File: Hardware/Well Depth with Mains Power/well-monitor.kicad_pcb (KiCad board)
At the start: 2 copper layers, 1 part, among them U1 ATmega328P-PU

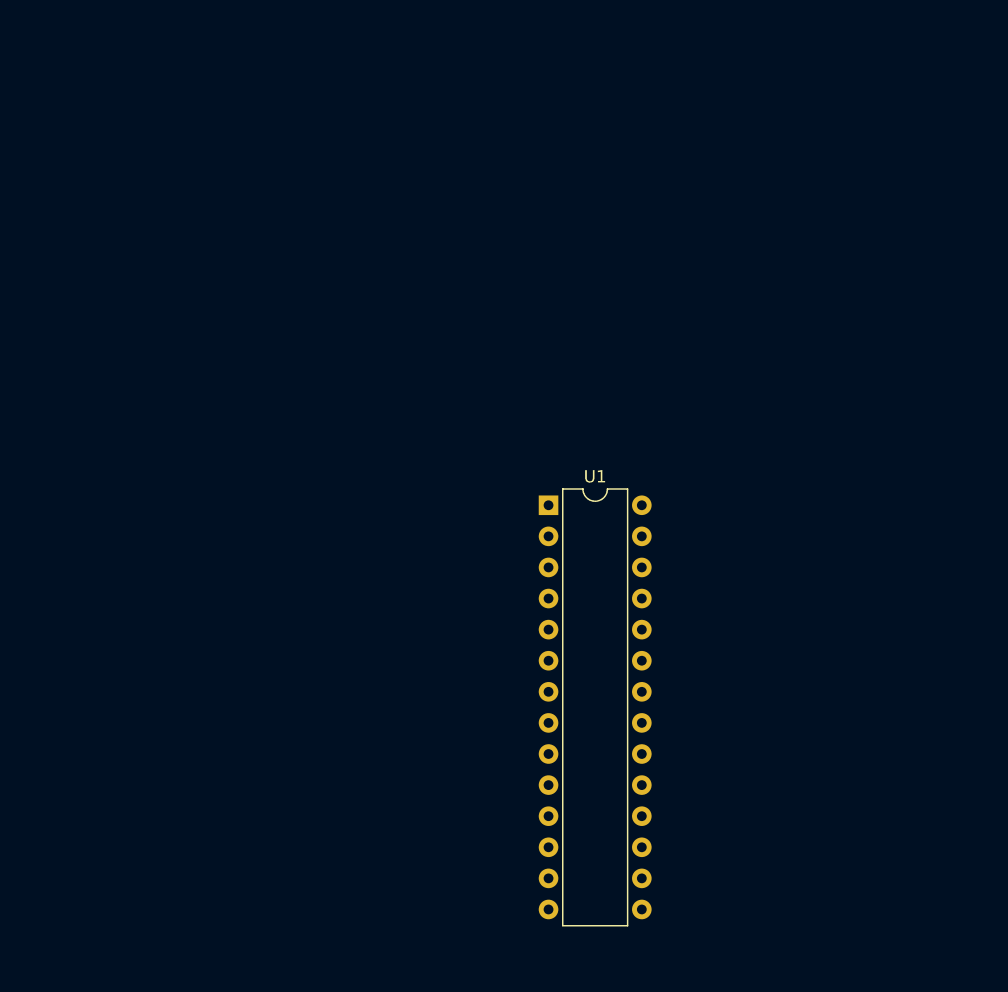
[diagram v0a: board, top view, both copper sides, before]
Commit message: First pass routing and DRC/ERC pass
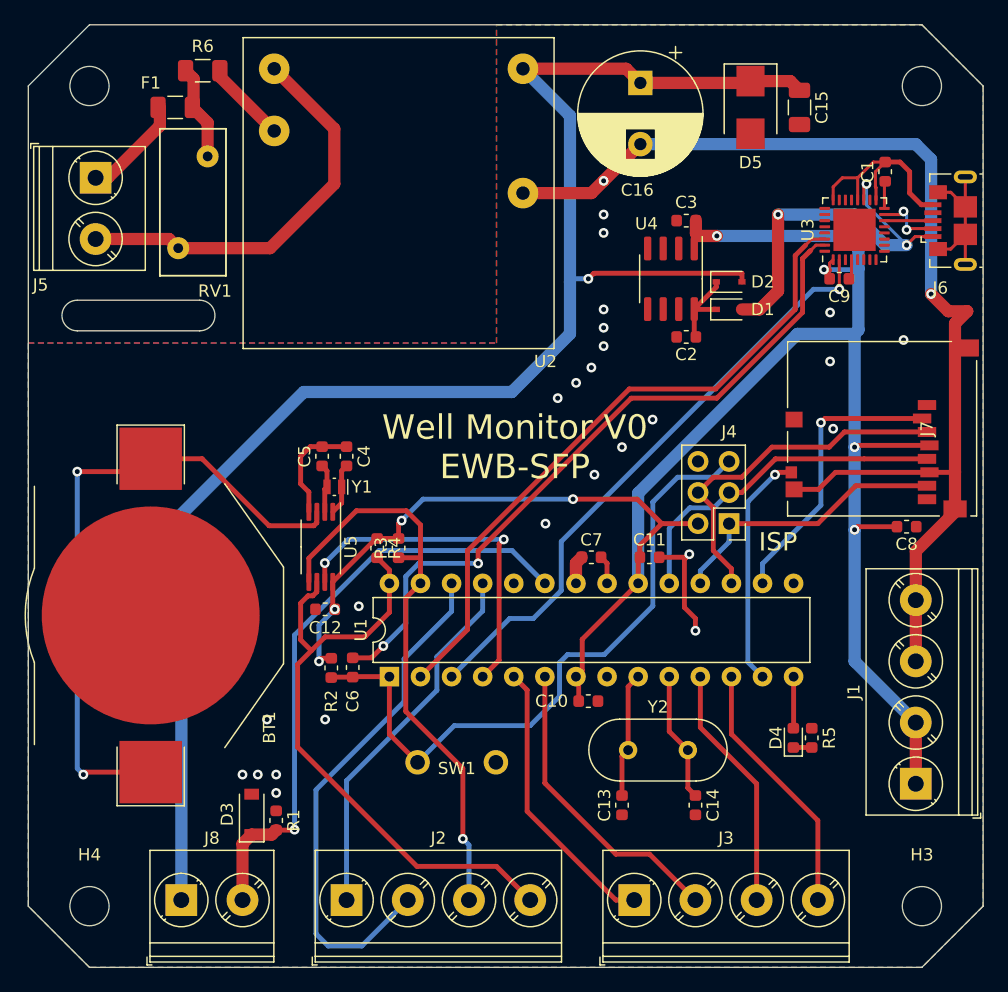
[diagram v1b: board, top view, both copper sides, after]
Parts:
- added BT1: Battery_Cell, well-monitor:BatteryHolder_Keystone_3002_1x2032, F.Cu at (105.0, 92.2)
- added C1: 1u, Capacitor_SMD:C_0603_1608Metric, F.Cu at (165.0, 56.0)
- added C10: 100n, Capacitor_SMD:C_0603_1608Metric, F.Cu at (140.8, 99.2)
- added C11: 100n, Capacitor_SMD:C_0603_1608Metric, F.Cu at (145.8, 87.5)
- added C12: 100n, Capacitor_SMD:C_0603_1608Metric, F.Cu at (119.2, 91.8)
- added C13: 10p, Capacitor_SMD:C_0603_1608Metric, F.Cu at (143.5, 107.8)
- added C14: 10p, Capacitor_SMD:C_0603_1608Metric, F.Cu at (149.5, 107.8)
- added C15: 1u, Capacitor_SMD:C_1206_3216Metric, F.Cu at (158.0, 50.8)
- added C16: 68u, Capacitor_THT:CP_Radial_D10.0mm_P5.00mm, F.Cu at (145.0, 48.8)
- added C2: 1u, Capacitor_SMD:C_0603_1608Metric, F.Cu at (148.8, 69.5)
- added C3: 1u, Capacitor_SMD:C_0603_1608Metric, F.Cu at (148.8, 60.0)
- added C4: 10p, Capacitor_SMD:C_0603_1608Metric, F.Cu at (121.0, 79.2)
- added C5: 10p, Capacitor_SMD:C_0603_1608Metric, F.Cu at (119.0, 79.2)
- added C6: 100n, Capacitor_SMD:C_0603_1608Metric, F.Cu at (121.5, 96.5)
- added C7: 100n, Capacitor_SMD:C_0603_1608Metric, F.Cu at (141.0, 87.5)
- added C8: 100n, Capacitor_SMD:C_0603_1608Metric, F.Cu at (166.8, 85.0)
- added C9: 100n, Capacitor_SMD:C_0603_1608Metric, F.Cu at (161.2, 64.8)
- added D1: CUS10S30, Diode_SMD:D_SOD-323, F.Cu at (152.2, 67.2)
- added D2: CUS10S30, Diode_SMD:D_SOD-323, F.Cu at (152.2, 65.0)
- added D3: 3.3, Diode_SMD:D_SOD-123, F.Cu at (113.2, 108.5)
- added D4: LED_Small, LED_SMD:LED_0603_1608Metric, F.Cu at (157.5, 102.2)
- added D5: SMBJ30A, Diode_SMD:D_SMB, F.Cu at (154.0, 50.8)
- added F1: 1, Fuse:Fuse_1206_3216Metric, F.Cu at (107.0, 50.8)
- added H1: MountingHole, MountingHole:MountingHole_3.2mm_M3, F.Cu at (100.0, 49.0)
- added H2: MountingHole, MountingHole:MountingHole_3.2mm_M3, F.Cu at (168.0, 49.0)
- added H3: MountingHole, MountingHole:MountingHole_3.2mm_M3, F.Cu at (168.0, 116.0)
- added H4: MountingHole, MountingHole:MountingHole_3.2mm_M3, F.Cu at (100.0, 116.0)
- added J1: Screw_Terminal_01x04, well-monitor:TerminalBlock_Phoenix_PT-1,5-4-5.0-H_1x04_P5.00mm_Horizontal, F.Cu at (167.5, 106.0)
- added J2: Screw_Terminal_01x04, well-monitor:TerminalBlock_Phoenix_PT-1,5-4-5.0-H_1x04_P5.00mm_Horizontal, F.Cu at (121.0, 115.5)
- added J3: Screw_Terminal_01x04, well-monitor:TerminalBlock_Phoenix_PT-1,5-4-5.0-H_1x04_P5.00mm_Horizontal, F.Cu at (144.5, 115.5)
- added J4: ISP Header, Connector_PinHeader_2.54mm:PinHeader_2x03_P2.54mm_Vertical, F.Cu at (152.2, 84.8)
- added J5: Screw_Terminal_01x02, well-monitor:TerminalBlock_Phoenix_PT-1,5-2-5.0-H_1x02_P5.00mm_Horizontal, F.Cu at (100.5, 56.5)
- added J6: USB_B_Micro, well-monitor:USB_Micro-B_GCT_USB3076-30-A, F.Cu at (170.3, 60.0)
- added J7: Micro_SD_Card, well-monitor:MEM2051-00-195-00-A, F.Cu at (164.8, 77.0)
- added J8: SENSOR, well-monitor:TerminalBlock_Phoenix_PT-1,5-2-5.0-H_1x02_P5.00mm_Horizontal, F.Cu at (107.5, 115.5)
- added R1: 150, Resistor_SMD:R_0603_1608Metric, F.Cu at (115.2, 109.0)
- added R2: 10k, Resistor_SMD:R_0603_1608Metric, F.Cu at (119.8, 96.5)
- added R3: 10k, Resistor_SMD:R_0603_1608Metric, F.Cu at (125.2, 86.8)
- added R4: 10k, Resistor_SMD:R_0603_1608Metric, F.Cu at (123.5, 86.8)
- added R5: 330, Resistor_SMD:R_0603_1608Metric, F.Cu at (159.0, 102.2)
- added R6: 12, Resistor_SMD:R_1206_3216Metric, F.Cu at (109.2, 47.8)
- added RV1: S10K350, Varistor:RV_Disc_D12mm_W5.4mm_P7.5mm, F.Cu at (107.2, 62.2)
- added SW1: SW_Push, well-monitor:PTS636-SP43-LFS, F.Cu at (130.0, 104.2)
- added U2: PSK-5D-24, well-monitor:PSK-5D-24, F.Cu at (125.2, 57.8)
- added U3: CY7C65213A-32LTXI, Package_DFN_QFN:QFN-32-1EP_5x5mm_P0.5mm_EP3.45x3.45mm, F.Cu at (162.5, 60.8)
- added U4: L78L33_SO8, Package_SO:SOIC-8_3.9x4.9mm_P1.27mm, F.Cu at (147.5, 64.8)
- added U5: MCP7940N-xMS, Package_SO:TSSOP-8_4.4x3mm_P0.65mm, F.Cu at (118.9, 86.7)
- added Y1: 32.768, Crystal:Crystal_SMD_MicroCrystal_CM9V-T1A-2Pin_1.6x1.0mm, F.Cu at (120.0, 81.8)
- added Y2: 16Meg, Crystal:Crystal_HC49-U_Vertical, F.Cu at (144.0, 103.2)
- moved U1 19.1 mm to (124.5, 97.2), turned to 90 degrees
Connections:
- U1 pad 1: (no net) -> /~RESET
- U1 pad 10: (no net) -> Net-(C14-Pad1)
- U1 pad 11: (no net) -> /GPIO_6
- U1 pad 12: (no net) -> /GPIO_7
- U1 pad 13: (no net) -> /SD_~DET
- U1 pad 14: (no net) -> Net-(D4-Pad2)
- U1 pad 16: (no net) -> /~CS
- U1 pad 17: (no net) -> /SDO
- U1 pad 18: (no net) -> /SDI
- U1 pad 19: (no net) -> /SCK
- U1 pad 2: (no net) -> /RX
- U1 pad 21: (no net) -> Net-(C7-Pad2)
- U1 pad 23: (no net) -> /DEPTH_SENSE
- U1 pad 25: (no net) -> /GPIO_0
- U1 pad 26: (no net) -> /GPIO_1
- U1 pad 27: (no net) -> /GPIO_2
- U1 pad 28: (no net) -> /GPIO_3
- U1 pad 3: (no net) -> /TX
- U1 pad 4: (no net) -> /RTC_MFP
- U1 pad 5: (no net) -> /GPIO_4
- U1 pad 6: (no net) -> /GPIO_5
- U1 pad 9: (no net) -> Net-(C13-Pad2)
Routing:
- net +3V3: track 0.00 -> 168.1 mm, vias 0 -> 8
- net GND: track 0.00 -> 134.1 mm, vias 0 -> 28
- net +24V: track 0.00 -> 131.1 mm, vias 0 -> 1
- net /DTR: track 0.00 -> 58.1 mm, vias 0 -> 2
- net /~RESET: track 0.00 -> 55.0 mm
- net /RX: track 0.00 -> 54.2 mm
- net Net-(BT1-Pad1): track 0.00 -> 53.8 mm, vias 0 -> 2
- net /GPIO_3: track 0.00 -> 51.8 mm
- net /DEPTH_SENSE: track 0.00 -> 49.6 mm, vias 0 -> 1
- net /TX: track 0.00 -> 49.6 mm, vias 0 -> 1
- net /GPIO_2: track 0.00 -> 48.2 mm, vias 0 -> 1
- net /GPIO_1: track 0.00 -> 42.7 mm
- net Net-(J5-Pad2): track 0.00 -> 33.4 mm
- net +5V: track 0.00 -> 31.6 mm, vias 0 -> 3
- net /GPIO_0: track 0.00 -> 30.5 mm
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- added copper zone on B.Cu, net GND
- added copper zone on F.Cu, net GND
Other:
- board outline added: 78 x 77 mm
- board text added: "+"
- board text added: "+3V3"
- board text added: "-"
- board text added: "AC 115-240 50-60Hz"
- board text added: "DEPTH"
- board text added: "GND"
- board text added: "GPIO"
- board text added: "ISP"
- board text added: "L"
- board text added: "N"
- board text added: "Well Monitor V0 EWB-SFP"

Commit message: Received hardware, started implementing software
Arduino IDE compatibility works, and SD card data logging has been tested and is functional.
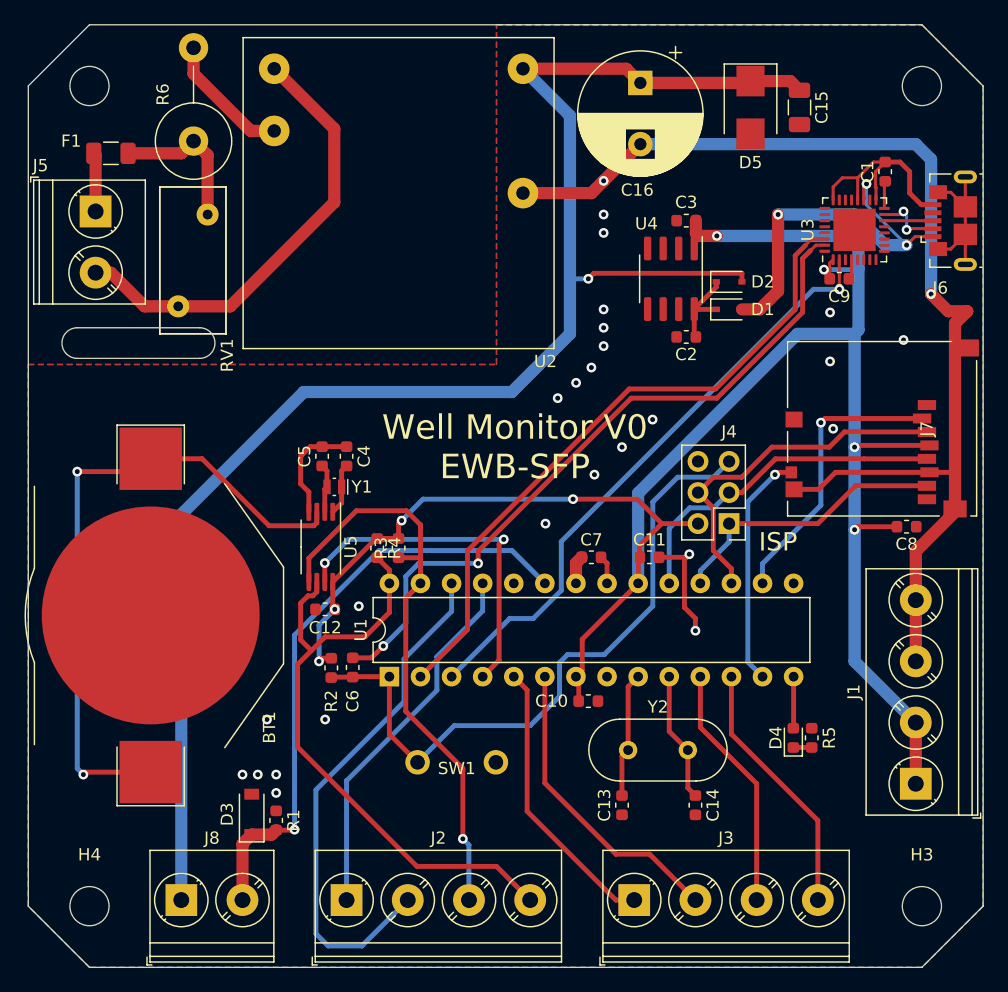
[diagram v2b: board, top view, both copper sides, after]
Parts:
- R6: footprint Resistor_SMD:R_1206_3216Metric -> Resistor_THT:R_Axial_DIN0617_L17.0mm_D6.0mm_P7.62mm_Vertical
- moved F1 6.45 mm to (101.8, 54.5)
- moved R6 5.80 mm to (108.5, 53.5), turned to 90 degrees
- moved RV1 4.75 mm to (107.2, 67.0)
- moved J5 2.75 mm to (100.5, 59.2)
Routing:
- net Net-(F1-Pad1): track 7.75 -> 12.2 mm
- net Net-(R6-Pad2): track 6.76 -> 10.6 mm
- net Net-(F1-Pad2): track 8.61 -> 4.81 mm
- net Net-(J5-Pad2): track 33.4 -> 37.1 mm
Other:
- outline, holes or cut-outs redrawn

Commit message: V1 (Fix issues with V0)
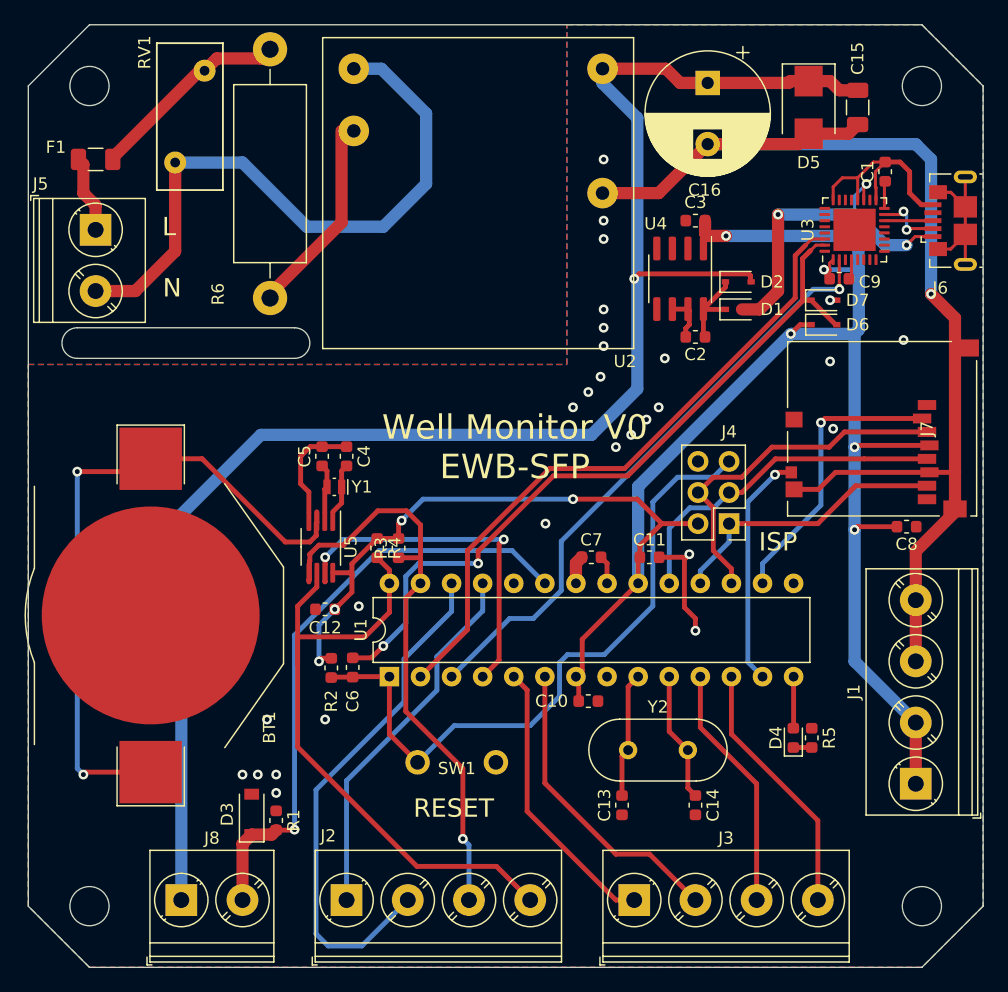
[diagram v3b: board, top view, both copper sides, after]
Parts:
- added D6: CUS10S30, Diode_SMD:D_SOD-323, F.Cu at (160.0, 68.5)
- added D7: CUS10S30, Diode_SMD:D_SOD-323, F.Cu at (160.0, 66.5)
- R6: footprint Resistor_THT:R_Axial_DIN0617_L17.0mm_D6.0mm_P7.62mm_Vertical -> Resistor_THT:R_Axial_DIN0614_L14.3mm_D5.7mm_P20.32mm_Horizontal
- U5: footprint Package_SO:TSSOP-8_4.4x3mm_P0.65mm -> Package_SO:MSOP-8_3x3mm_P0.65mm
- moved RV1 11.8 mm to (107.0, 55.2)
- moved R6 9.76 mm to (114.8, 46.0), turned to 270 degrees
- moved U2 6.50 mm to (131.8, 57.8)
- moved C16 5.50 mm to (150.5, 48.8)
- moved C15 4.75 mm to (162.8, 50.8)
- moved D5 4.75 mm to (158.8, 50.8)
- moved J5 1.50 mm to (100.5, 60.8)
- moved F1 1.35 mm to (100.5, 55.0)
- moved C2 0.75 mm to (149.5, 69.5)
- moved C3 0.75 mm to (149.5, 60.0)
- moved D1 0.75 mm to (153.0, 67.2)
- moved D2 0.75 mm to (153.0, 65.0)
- moved U4 0.75 mm to (148.2, 64.8)
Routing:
- net Net-(J5-Pad2): track 37.1 -> 52.4 mm
- net GND: track 134.1 -> 143.1 mm, vias 28 -> 29
- net Net-(R6-Pad2): track 10.6 -> 16.9 mm
- net Net-(F1-Pad1): track 12.2 -> 16.7 mm
- net /DTR: track 58.1 -> 61.2 mm
- net +3V3: track 168.1 -> 171.1 mm, vias 8 -> 9
- net /GPIO_3: track 51.8 -> 53.8 mm
- net +5V: track 31.6 -> 33.2 mm
- net Net-(BT1-Pad1): track 53.8 -> 55.5 mm
- net Net-(F1-Pad2): track 4.81 -> 6.33 mm
- net +24V: track 131.1 -> 132.3 mm
- net /RX: track 54.2 -> 53.6 mm
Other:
- outline, holes or cut-outs redrawn
- board text added: "1x 2032 3V"
- board text added: "AC 115-240 50-60Hz Disconnect before servicing"
- board text added: "RESET"
- board text removed: "AC 115-240 50-60Hz"

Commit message: Added RTC functionality
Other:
- board text added: "Well Monitor V1 EWB-SFP"
- board text removed: "Well Monitor V0 EWB-SFP"
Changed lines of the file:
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@@
     (effects (font (size 1.5 1.5) (thickness 0.3)))
   )
-  (gr_text "Well Monitor V0\nEWB-SFP" (at 134.75 78.5) (layer F.SilkS)
+  (gr_text "Well Monitor V1\nEWB-SFP" (at 134.75 78.5) (layer F.SilkS)
     (effects (font (size 2 2) (thickness 0.3)))
   )

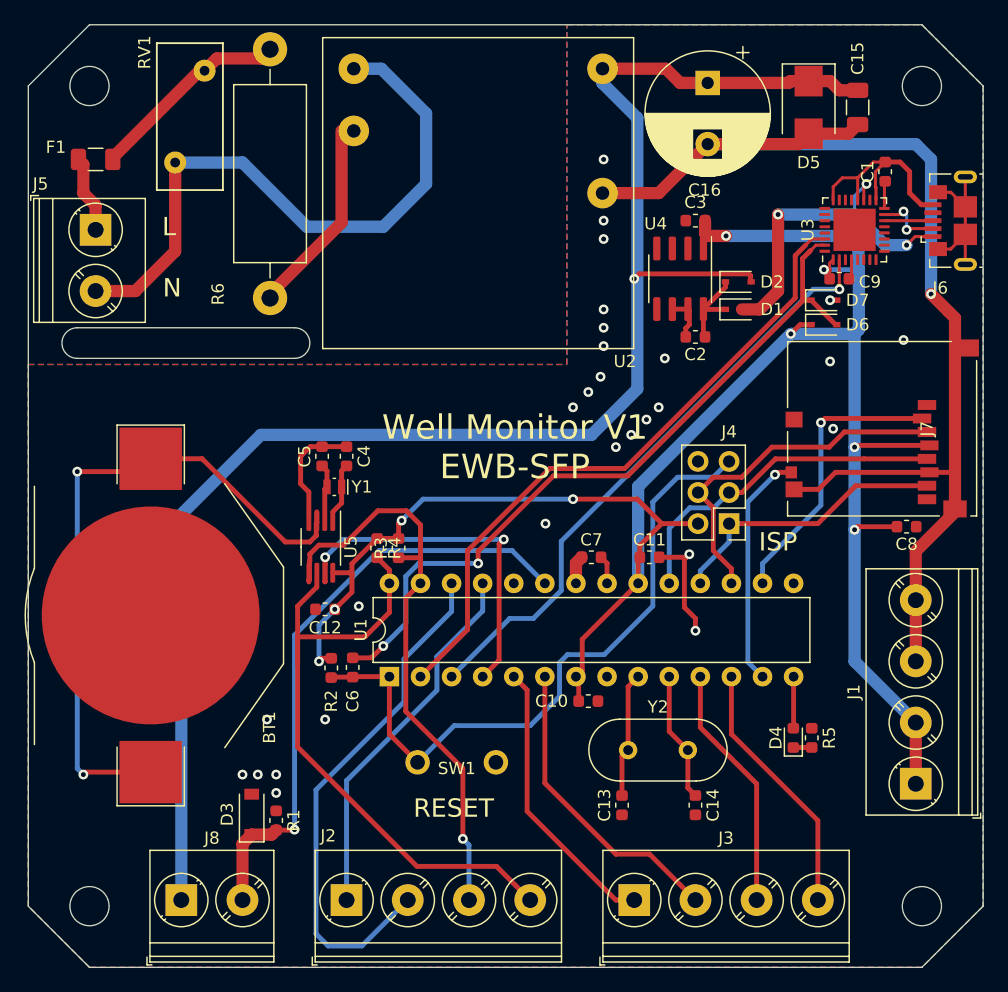
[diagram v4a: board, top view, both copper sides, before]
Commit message: Well Monitor: Update to newest KiCAD version
Also updated CAM files
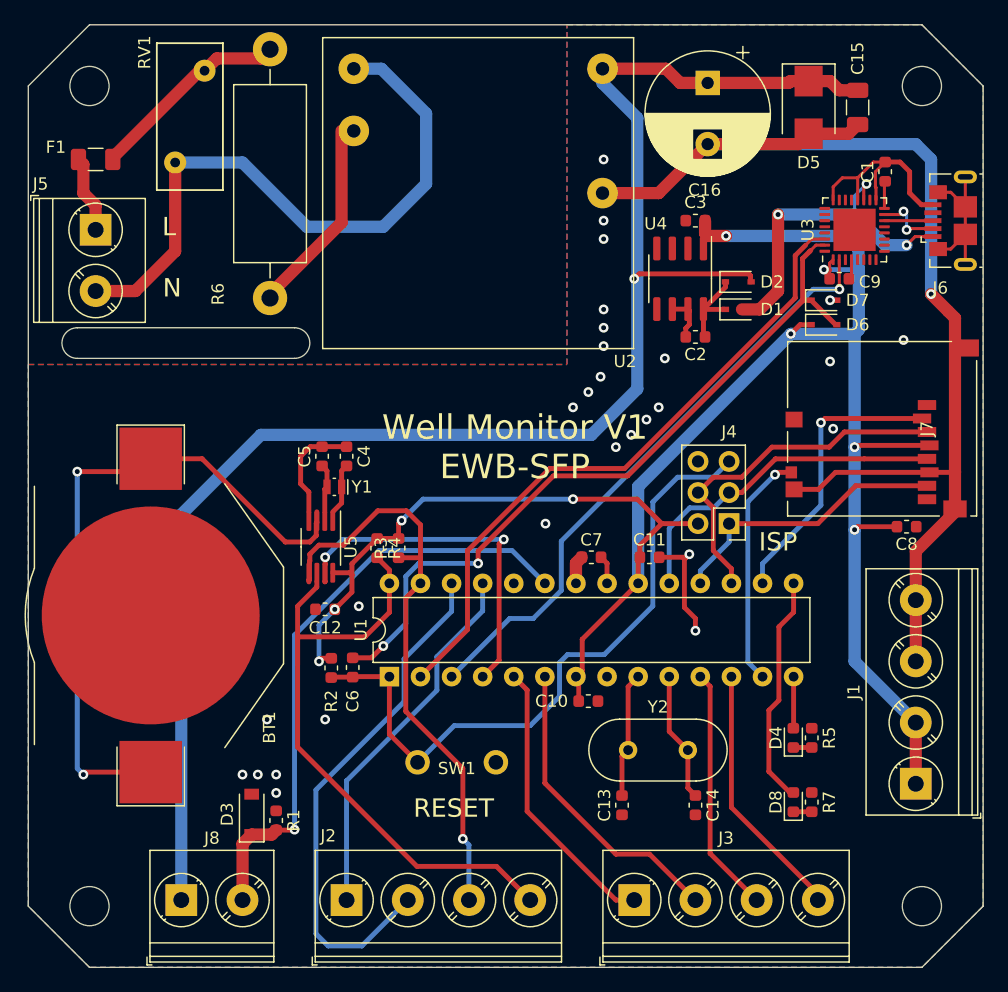
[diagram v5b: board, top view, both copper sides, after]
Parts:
- added D8: LED_Small, LED_SMD:LED_0603_1608Metric, F.Cu at (157.5, 107.5)
- added R7: 330, Resistor_SMD:R_0603_1608Metric, F.Cu at (159.0, 107.5)
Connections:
- net /SD_~DET renamed /SD_~{DET}
- net /~CS renamed /~{CS}
- net /~RESET renamed /~{RESET}
- U1 pad 15: (no net) -> Net-(D8-Pad2)
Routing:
- net Net-(D8-Pad2): track 0.00 -> 18.9 mm
- net Net-(D8-Pad1): track 0.00 -> 1.50 mm
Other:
- net class Default removed
